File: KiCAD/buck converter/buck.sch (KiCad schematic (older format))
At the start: 17 parts, among them P1 VIN, P2 VOUT, Q1 Q_PMOS_DGS, U1 LTC1771

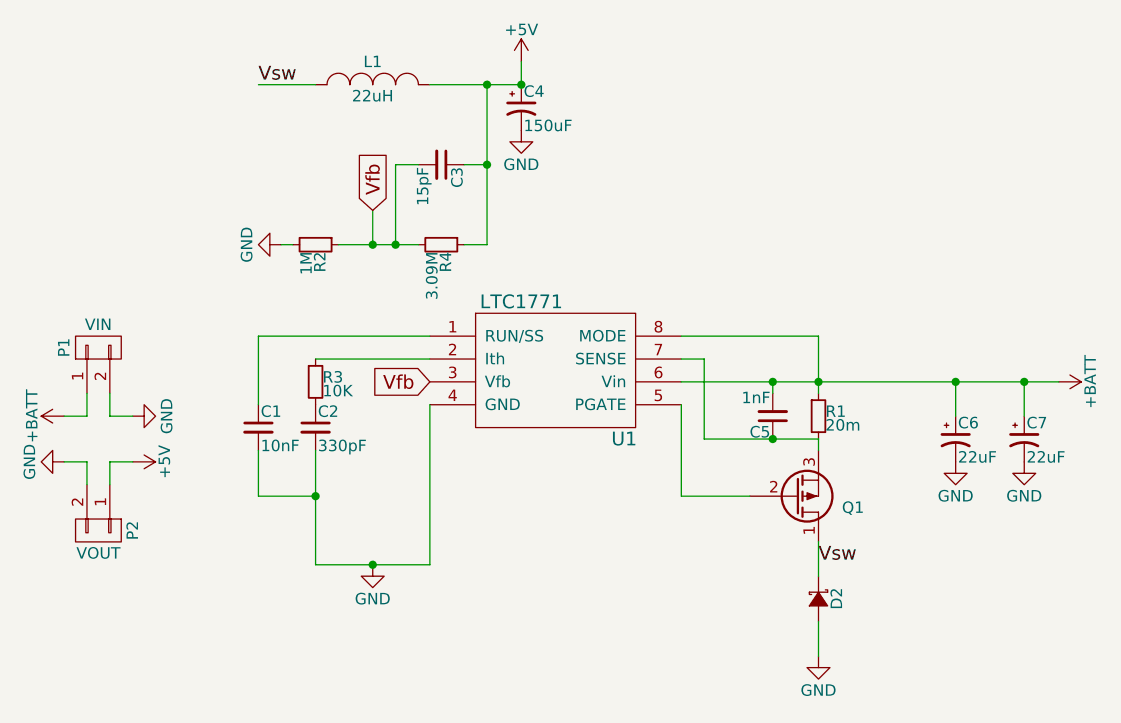
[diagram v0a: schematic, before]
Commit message: Improved the buck converter board layout
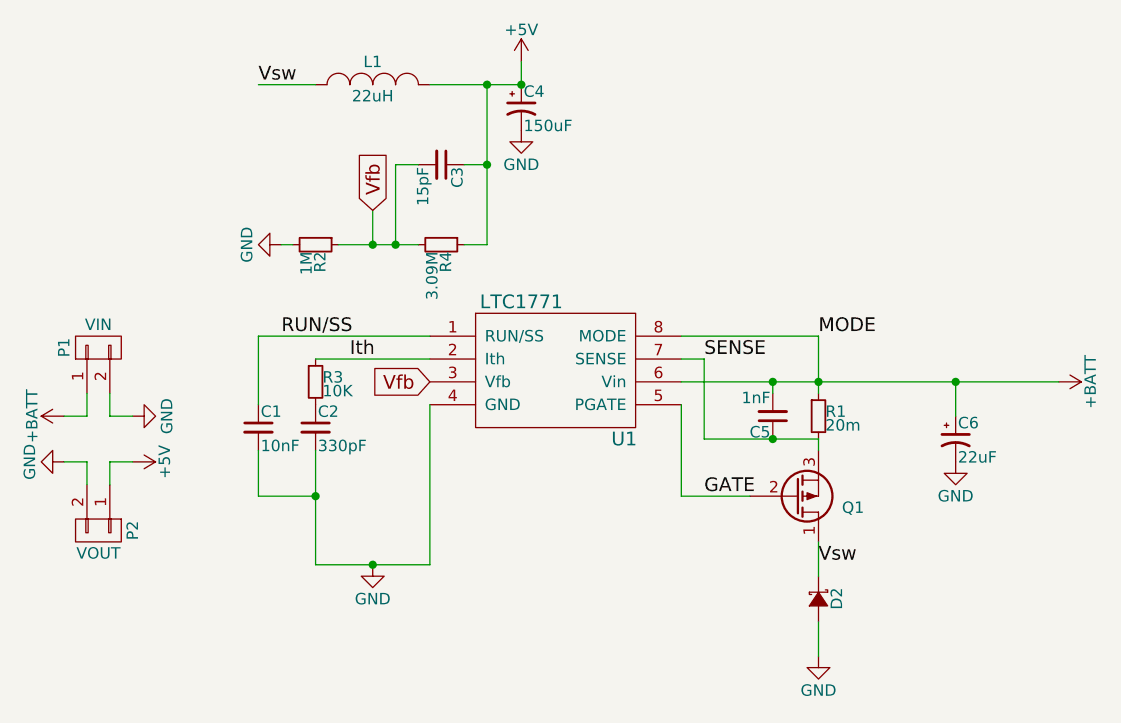
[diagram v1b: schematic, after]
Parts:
- removed C7: 22uF, Capacitors_SMD:CP_Elec_6.3x5.3, symbol CP1_Small
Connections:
- net SENSE: now reaches C5.1, Q1.3 (S), R1.2, U1.7 (SENSE)
- net GATE: now reaches Q1.2 (G), U1.5 (PGATE)
- net Ith: now reaches R3.1, U1.2 (Ith)
- net RUN/SS: now reaches C1.1, U1.1 (RUN/SS)
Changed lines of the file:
@@
-$EndComp
-$Comp
-L CP1_Small C7
-U 1 1 58964A17
-P 7800 4150
-F 0 "C7" H 7810 4220 50  0000 L CNN
-F 1 "22uF" H 7810 4070 50  0000 L CNN
-F 2 "Capacitors_SMD:CP_Elec_6.3x5.3" H 7800 4150 50  0001 C CNN
-F 3 "" H 7800 4150 50  0000 C CNN
-	1    7800 4150
-	1    0    0    -1
 $EndComp
 $Comp
@@
 	5200 4000 5200 4700
 Connection ~ 7500 3900
-Connection ~ 7800 3900
-Wire Wire Line
-	7800 4050 7800 3900
 Wire Wire Line
 	7500 3900 7500 4050
@@
 	1    0    0    -1
 $EndComp
-$Comp
-L GND #PWR07
-U 1 1 58966331
-P 7800 4250
-F 0 "#PWR07" H 7800 4000 50  0001 C CNN
-F 1 "GND" H 7800 4100 50  0000 C CNN
-F 2 "" H 7800 4250 50  0000 C CNN
-F 3 "" H 7800 4250 50  0000 C CNN
-	1    7800 4250
-	1    0    0    -1
-$EndComp
 Wire Wire Line
 	6300 3700 6900 3700
@@
 	1    0    0    -1
 $EndComp
+Text Label 6400 3800 0    60   ~ 0
+SENSE
+Text Label 6900 3700 0    60   ~ 0
+MODE
+Text Label 6400 4400 0    60   ~ 0
+GATE
+Text Label 4850 3800 0    60   ~ 0
+Ith
+Text Label 4550 3700 0    60   ~ 0
+RUN/SS
 $EndSCHEMATC

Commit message: Updated board layout
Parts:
- added JP1: BURST, Connectors:PINHEAD1-3, symbol Jumper_NC_Dual
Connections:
- net +BATT: now also JP1.3; no longer U1.8 (MODE)
- net GND: now also JP1.1
- new net MODE: JP1.2, U1.8 (MODE)
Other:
- moved on the sheet: C5
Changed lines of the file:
@@
 F 3 "" H 6900 4050 50  0000 C CNN
 	1    6900 4050
-	1    0    0    -1
+	1    0    0    1
 $EndComp
 $Comp
@@
 L C_Small C5
 U 1 1 58964849
-P 6700 4050
-F 0 "C5" H 6710 4120 50  0000 L CNN
-F 1 "1nF" H 6710 3970 50  0000 L CNN
-F 2 "Capacitors_SMD:C_0805_HandSoldering" H 6700 4050 50  0001 C CNN
-F 3 "" H 6700 4050 50  0000 C CNN
-	1    6700 4050
-	-1   0    0    1
+P 7250 3800
+F 0 "C5" H 7260 3870 50  0000 L CNN
+F 1 "1nF" H 7260 3720 50  0000 L CNN
+F 2 "Capacitors_SMD:C_0805_HandSoldering" H 7250 3800 50  0001 C CNN
+F 3 "" H 7250 3800 50  0000 C CNN
+	1    7250 3800
+	0    -1   -1   0
 $EndComp
 $Comp
@@
 Connection ~ 7500 3900
 Wire Wire Line
-	7500 3900 7500 4050
+	7500 3800 7500 4050
 Wire Wire Line
 	6300 4000 6300 4400
@@
 	6300 4400 6600 4400
 Wire Wire Line
-	6900 3700 6900 3950
-Connection ~ 6900 3900
-Wire Wire Line
-	6900 4150 6900 4200
-Wire Wire Line
-	6400 4150 6400 3800
-Wire Wire Line
-	6400 3800 6300 3800
+	6300 3800 7150 3800
 Wire Wire Line
 	6900 4750 6900 4600
 $Comp
-L GND #PWR06
+L GND #PWR05
 U 1 1 589662F9
 P 7500 4250
-F 0 "#PWR06" H 7500 4000 50  0001 C CNN
+F 0 "#PWR05" H 7500 4000 50  0001 C CNN
 F 1 "GND" H 7500 4100 50  0000 C CNN
 F 2 "" H 7500 4250 50  0000 C CNN
@@
 Wire Wire Line
 	6300 3700 6900 3700
-Connection ~ 6700 3900
-Wire Wire Line
-	6700 3950 6700 3900
-Wire Wire Line
-	6400 4150 6900 4150
-Connection ~ 6700 4150
 Wire Wire Line
 	4700 3800 5200 3800
@@
 Connection ~ 4950 3300
 $Comp
-L GND #PWR08
+L GND #PWR06
 U 1 1 58967FFD
 P 4550 3300
-F 0 "#PWR08" H 4550 3050 50  0001 C CNN
+F 0 "#PWR06" H 4550 3050 50  0001 C CNN
 F 1 "GND" H 4550 3150 50  0000 C CNN
 F 2 "" H 4550 3300 50  0000 C CNN
@@
 Connection ~ 5450 2600
 $Comp
-L GND #PWR09
+L GND #PWR07
 U 1 1 58968BDB
 P 5600 2800
-F 0 "#PWR09" H 5600 2550 50  0001 C CNN
+F 0 "#PWR07" H 5600 2550 50  0001 C CNN
 F 1 "GND" H 5600 2650 50  0000 C CNN
 F 2 "" H 5600 2800 50  0000 C CNN
@@
 	5200 2600 5600 2600
 $Comp
-L +5V #PWR010
+L +5V #PWR08
 U 1 1 58969042
 P 5600 2500
-F 0 "#PWR010" H 5600 2350 50  0001 C CNN
+F 0 "#PWR08" H 5600 2350 50  0001 C CNN
 F 1 "+5V" H 5600 2640 50  0000 C CNN
 F 2 "" H 5600 2500 50  0000 C CNN
@@
 	5600 2600 5600 2500
 $Comp
-L +5V #PWR011
+L +5V #PWR09
 U 1 1 589690C9
 P 3900 4250
-F 0 "#PWR011" H 3900 4100 50  0001 C CNN
+F 0 "#PWR09" H 3900 4100 50  0001 C CNN
 F 1 "+5V" H 3900 4390 50  0000 C CNN
 F 2 "" H 3900 4250 50  0000 C CNN
@@
 	3800 4250 3900 4250
 $Comp
-L GND #PWR012
+L GND #PWR010
 U 1 1 5896914A
 P 3600 4250
-F 0 "#PWR012" H 3600 4000 50  0001 C CNN
+F 0 "#PWR010" H 3600 4000 50  0001 C CNN
 F 1 "GND" H 3600 4100 50  0000 C CNN
 F 2 "" H 3600 4250 50  0000 C CNN
@@
 	6900 5100 6900 4950
 $Comp
-L GND #PWR05
+L GND #PWR011
 U 1 1 58965DDE
 P 6900 5100
-F 0 "#PWR05" H 6900 4850 50  0001 C CNN
+F 0 "#PWR011" H 6900 4850 50  0001 C CNN
 F 1 "GND" H 6900 4950 50  0000 C CNN
 F 2 "" H 6900 5100 50  0000 C CNN
@@
 Text Label 4550 3700 0    60   ~ 0
 RUN/SS
+$Comp
+L Jumper_NC_Dual JP1
+U 1 1 5898D624
+P 6900 3400
+F 0 "JP1" H 6950 3300 50  0000 L CNN
+F 1 "BURST" H 6900 3500 50  0000 C BNN
+F 2 "Connectors:PINHEAD1-3" H 6900 3400 50  0001 C CNN
+F 3 "" H 6900 3400 50  0000 C CNN
+	1    6900 3400
+	1    0    0    -1
+$EndComp
+$Comp
+L +BATT #PWR012
+U 1 1 5898D713
+P 7150 3400
+F 0 "#PWR012" H 7150 3250 50  0001 C CNN
+F 1 "+BATT" H 7150 3540 50  0000 C CNN
+F 2 "" H 7150 3400 50  0000 C CNN
+F 3 "" H 7150 3400 50  0000 C CNN
+	1    7150 3400
+	0    1    1    0
+$EndComp
+$Comp
+L GND #PWR013
+U 1 1 5898D751
+P 6650 3400
+F 0 "#PWR013" H 6650 3150 50  0001 C CNN
+F 1 "GND" H 6650 3250 50  0000 C CNN
+F 2 "" H 6650 3400 50  0000 C CNN
+F 3 "" H 6650 3400 50  0000 C CNN
+	1    6650 3400
+	0    1    1    0
+$EndComp
+Wire Wire Line
+	6900 3700 6900 3500
+Wire Wire Line
+	6900 3800 6900 3950
+Connection ~ 6900 3800
+Wire Wire Line
+	7350 3800 7500 3800
+Wire Wire Line
+	6900 4250 6900 4200
+Wire Wire Line
+	6900 4200 6500 4200
+Wire Wire Line
+	6500 4200 6500 3800
+Connection ~ 6500 3800
+Wire Wire Line
+	6900 4150 7300 4150
+Wire Wire Line
+	7300 4150 7300 3900
+Connection ~ 7300 3900
 $EndSCHEMATC

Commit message: Updated inductor footprint
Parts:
- L1: footprint Buck:inductor_th_10mm -> Buck:14mm-Inductor
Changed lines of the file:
@@
 F 0 "L1" H 4950 2700 50  0000 C CNN
 F 1 "22uH" H 4950 2550 50  0000 C CNN
-F 2 "Buck:inductor_th_10mm" H 4950 2600 50  0001 C CNN
+F 2 "Buck:14mm-Inductor" H 4950 2600 50  0001 C CNN
 F 3 "" H 4950 2600 50  0000 C CNN
 	1    4950 2600

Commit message: Updated schematic, PCB, amd BOM
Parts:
- removed JP1: BURST, Connectors:PINHEAD1-3, symbol Jumper_NC_Dual
- removed Q1: Q_PMOS_DGS, TO_SOT_Packages_SMD:SOT-23-6_Handsoldering, symbol Q_PMOS_DGS
- added U2: SI3421DV-T1-GE3, TO_SOT_Packages_SMD:SOT-23-6_Handsoldering, symbol SI3421DV-T1-GE3
- C4: value 150uF -> 330uF; footprint Capacitors_SMD:CP_Elec_6.3x5.8 -> Capacitors_SMD:CP_Elec_8x10
- D2: footprint Diodes_SMD:D_SOD-323_HandSoldering -> Diodes_SMD:D_SMB_Handsoldering
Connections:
- net MODE is gone; now on net GND: U1.8 (MODE)
- net GATE: now also U2.3 (G)
- net SENSE: now also U2.4 (S)
- net Vsw: now also U2.1 (D), U2.2 (D), U2.5 (D), U2.6 (D)
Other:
- moved on the sheet: D2
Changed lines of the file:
@@
 LIBS:roadrunner
 LIBS:tinkerforge
+LIBS:FET
 LIBS:buck-cache
 EELAYER 25 0
@@
 L D_Schottky_Small D2
 U 1 1 58962EBE
-P 6900 4850
-F 0 "D2" H 6850 4930 50  0000 L CNN
-F 1 "D_Schottky_Small" H 6620 4770 50  0001 L CNN
-F 2 "Diodes_SMD:D_SOD-323_HandSoldering" V 6900 4850 50  0001 C CNN
-F 3 "" V 6900 4850 50  0000 C CNN
-	1    6900 4850
-	0    1    1    0
+P 5900 4700
+F 0 "D2" H 5850 4780 50  0000 L CNN
+F 1 "D_Schottky_Small" H 5620 4620 50  0001 L CNN
+F 2 "Diodes_SMD:D_SMB_Handsoldering" V 5900 4700 50  0001 C CNN
+F 3 "" V 5900 4700 50  0000 C CNN
+	1    5900 4700
+	-1   0    0    1
 $EndComp
 $Comp
@@
 $EndComp
 $Comp
-L Q_PMOS_DGS Q1
-U 1 1 589631E9
-P 6800 4400
-F 0 "Q1" H 7100 4450 50  0000 R CNN
-F 1 "Q_PMOS_DGS" H 7450 4350 50  0001 R CNN
-F 2 "TO_SOT_Packages_SMD:SOT-23-6_Handsoldering" H 7000 4500 50  0001 C CNN
-F 3 "" H 6800 4400 50  0000 C CNN
-	1    6800 4400
-	1    0    0    1
-$EndComp
-$Comp
 L INDUCTOR_SMALL L1
 U 1 1 5896391B
@@
 P 5600 2700
 F 0 "C4" H 5610 2770 50  0000 L CNN
-F 1 "150uF" H 5610 2620 50  0000 L CNN
-F 2 "Capacitors_SMD:CP_Elec_6.3x5.8" H 5600 2700 50  0001 C CNN
+F 1 "330uF" H 5610 2620 50  0000 L CNN
+F 2 "Capacitors_SMD:CP_Elec_8x10" H 5600 2700 50  0001 C CNN
 F 3 "" H 5600 2700 50  0000 C CNN
 	1    5600 2700
@@
 	7500 3800 7500 4050
 Wire Wire Line
-	6300 4000 6300 4400
-Wire Wire Line
-	6300 4400 6600 4400
-Wire Wire Line
 	6300 3800 7150 3800
 Wire Wire Line
-	6900 4750 6900 4600
+	6000 4700 7150 4700
 $Comp
 L GND #PWR05
@@
 	5450 2950 5350 2950
 Connection ~ 5450 2950
-Text Label 6900 4700 0    60   ~ 0
+Text Label 6050 4700 3    60   ~ 0
 Vsw
 Wire Wire Line
@@
 	3700 4250 3600 4250
 Wire Wire Line
-	6900 5100 6900 4950
-$Comp
-L GND #PWR011
-U 1 1 58965DDE
-P 6900 5100
-F 0 "#PWR011" H 6900 4850 50  0001 C CNN
-F 1 "GND" H 6900 4950 50  0000 C CNN
-F 2 "" H 6900 5100 50  0000 C CNN
-F 3 "" H 6900 5100 50  0000 C CNN
-	1    6900 5100
-	1    0    0    -1
-$EndComp
+	5650 4700 5800 4700
 Text Label 6400 3800 0    60   ~ 0
 SENSE
 Text Label 6900 3700 0    60   ~ 0
 MODE
-Text Label 6400 4400 0    60   ~ 0
-GATE
 Text Label 4850 3800 0    60   ~ 0
 Ith
@@
 RUN/SS
 $Comp
-L Jumper_NC_Dual JP1
-U 1 1 5898D624
-P 6900 3400
-F 0 "JP1" H 6950 3300 50  0000 L CNN
-F 1 "BURST" H 6900 3500 50  0000 C BNN
-F 2 "Connectors:PINHEAD1-3" H 6900 3400 50  0001 C CNN
-F 3 "" H 6900 3400 50  0000 C CNN
-	1    6900 3400
-	1    0    0    -1
-$EndComp
-$Comp
-L +BATT #PWR012
-U 1 1 5898D713
-P 7150 3400
-F 0 "#PWR012" H 7150 3250 50  0001 C CNN
-F 1 "+BATT" H 7150 3540 50  0000 C CNN
-F 2 "" H 7150 3400 50  0000 C CNN
-F 3 "" H 7150 3400 50  0000 C CNN
-	1    7150 3400
-	0    1    1    0
-$EndComp
-$Comp
-L GND #PWR013
+L GND #PWR011
 U 1 1 5898D751
-P 6650 3400
-F 0 "#PWR013" H 6650 3150 50  0001 C CNN
-F 1 "GND" H 6650 3250 50  0000 C CNN
-F 2 "" H 6650 3400 50  0000 C CNN
-F 3 "" H 6650 3400 50  0000 C CNN
-	1    6650 3400
-	0    1    1    0
+P 6900 3500
+F 0 "#PWR011" H 6900 3250 50  0001 C CNN
+F 1 "GND" H 6900 3350 50  0000 C CNN
+F 2 "" H 6900 3500 50  0000 C CNN
+F 3 "" H 6900 3500 50  0000 C CNN
+	1    6900 3500
+	-1   0    0    1
 $EndComp
 Wire Wire Line
@@
 	7350 3800 7500 3800
 Wire Wire Line
-	6900 4250 6900 4200
-Wire Wire Line
-	6900 4200 6500 4200
-Wire Wire Line
-	6500 4200 6500 3800
+	6500 3800 6500 4250
 Connection ~ 6500 3800
 Wire Wire Line
@@
 	7300 4150 7300 3900
 Connection ~ 7300 3900
+$Comp
+L GND #PWR012
+U 1 1 58965DDE
+P 5650 4700
+F 0 "#PWR012" H 5650 4450 50  0001 C CNN
+F 1 "GND" H 5650 4550 50  0000 C CNN
+F 2 "" H 5650 4700 50  0000 C CNN
+F 3 "" H 5650 4700 50  0000 C CNN
+	1    5650 4700
+	0    1    1    0
+$EndComp
+$Comp
+L SI3421DV-T1-GE3 U2
+U 1 1 58D46DD3
+P 6800 5050
+F 0 "U2" H 6700 5250 60  0000 C CNN
+F 1 "SI3421DV-T1-GE3" H 6800 4850 60  0000 C CNN
+F 2 "TO_SOT_Packages_SMD:SOT-23-6_Handsoldering" H 6800 4800 60  0001 C CNN
+F 3 "" H 6800 4800 60  0001 C CNN
+	1    6800 5050
+	1    0    0    -1
+$EndComp
+Wire Wire Line
+	6300 4000 6300 5150
+Wire Wire Line
+	6300 5150 6450 5150
+Text Label 6300 5150 0    60   ~ 0
+GATE
+Wire Wire Line
+	6450 4700 6450 5050
+Connection ~ 6450 4950
+Wire Wire Line
+	7150 4700 7150 5050
+Connection ~ 6450 4700
+Connection ~ 7150 4950
+Wire Wire Line
+	7150 5150 7300 5150
+Wire Wire Line
+	7300 5150 7300 4250
+Wire Wire Line
+	7300 4250 6500 4250
 $EndSCHEMATC

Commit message: Board design updated
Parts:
- added C7: 100nF, Capacitors_SMD:C_0805_HandSoldering, symbol C_Small
- C4: value 330uF -> 150uF; footprint Capacitors_SMD:CP_Elec_8x10 -> Capacitors_SMD:CP_Elec_6.3x7.7
- C6: value 22uF -> 56uF; footprint Capacitors_SMD:CP_Elec_6.3x5.3 -> Capacitors_SMD:CP_Elec_5x5.7
- D2: footprint Diodes_SMD:D_SMB_Handsoldering -> Diodes_SMD:D_SMA_Handsoldering
- R1: value 20m -> 33m
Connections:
- net +BATT: now also C7.1
- net GND: now also C7.2
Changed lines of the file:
@@
 F 0 "D2" H 5850 4780 50  0000 L CNN
 F 1 "D_Schottky_Small" H 5620 4620 50  0001 L CNN
-F 2 "Diodes_SMD:D_SMB_Handsoldering" V 5900 4700 50  0001 C CNN
+F 2 "Diodes_SMD:D_SMA_Handsoldering" V 5900 4700 50  0001 C CNN
 F 3 "" V 5900 4700 50  0000 C CNN
 	1    5900 4700
@@
 P 6900 4050
 F 0 "R1" H 6930 4070 50  0000 L CNN
-F 1 "20m" H 6930 4010 50  0000 L CNN
+F 1 "33m" H 6930 4010 50  0000 L CNN
 F 2 "Resistors_SMD:R_1206_HandSoldering" H 6900 4050 50  0001 C CNN
 F 3 "" H 6900 4050 50  0000 C CNN
@@
 P 7500 4150
 F 0 "C6" H 7510 4220 50  0000 L CNN
-F 1 "22uF" H 7510 4070 50  0000 L CNN
-F 2 "Capacitors_SMD:CP_Elec_6.3x5.3" H 7500 4150 50  0001 C CNN
+F 1 "56uF" H 7510 4070 50  0000 L CNN
+F 2 "Capacitors_SMD:CP_Elec_5x5.7" H 7500 4150 50  0001 C CNN
 F 3 "" H 7500 4150 50  0000 C CNN
 	1    7500 4150
@@
 P 5600 2700
 F 0 "C4" H 5610 2770 50  0000 L CNN
-F 1 "330uF" H 5610 2620 50  0000 L CNN
-F 2 "Capacitors_SMD:CP_Elec_8x10" H 5600 2700 50  0001 C CNN
+F 1 "150uF" H 5610 2620 50  0000 L CNN
+F 2 "Capacitors_SMD:CP_Elec_6.3x7.7" H 5600 2700 50  0001 C CNN
 F 3 "" H 5600 2700 50  0000 C CNN
 	1    5600 2700
@@
 	3700 4050 3600 4050
 $Comp
-L GND #PWR01
+L GND #PWR3
 U 1 1 58964DDE
 P 3900 4050
-F 0 "#PWR01" H 3900 3800 50  0001 C CNN
+F 0 "#PWR3" H 3900 3800 50  0001 C CNN
 F 1 "GND" H 3900 3900 50  0000 C CNN
 F 2 "" H 3900 4050 50  0000 C CNN
@@
 $EndComp
 $Comp
-L +BATT #PWR02
+L +BATT #PWR1
 U 1 1 58964E10
 P 3600 4050
-F 0 "#PWR02" H 3600 3900 50  0001 C CNN
+F 0 "#PWR1" H 3600 3900 50  0001 C CNN
 F 1 "+BATT" H 3600 4190 50  0000 C CNN
 F 2 "" H 3600 4050 50  0000 C CNN
@@
 $EndComp
 $Comp
-L +BATT #PWR03
+L +BATT #PWR13
 U 1 1 5896507A
 P 7950 3900
-F 0 "#PWR03" H 7950 3750 50  0001 C CNN
+F 0 "#PWR13" H 7950 3750 50  0001 C CNN
 F 1 "+BATT" H 7950 4040 50  0000 C CNN
 F 2 "" H 7950 3900 50  0000 C CNN
@@
 	6300 3900 7950 3900
 $Comp
-L GND #PWR04
+L GND #PWR6
 U 1 1 589650C7
 P 4950 4700
-F 0 "#PWR04" H 4950 4450 50  0001 C CNN
+F 0 "#PWR6" H 4950 4450 50  0001 C CNN
 F 1 "GND" H 4950 4550 50  0000 C CNN
 F 2 "" H 4950 4700 50  0000 C CNN
@@
 	6000 4700 7150 4700
 $Comp
-L GND #PWR05
+L GND #PWR11
 U 1 1 589662F9
 P 7500 4250
-F 0 "#PWR05" H 7500 4000 50  0001 C CNN
+F 0 "#PWR11" H 7500 4000 50  0001 C CNN
 F 1 "GND" H 7500 4100 50  0000 C CNN
 F 2 "" H 7500 4250 50  0000 C CNN
@@
 Connection ~ 4950 3300
 $Comp
-L GND #PWR06
+L GND #PWR5
 U 1 1 58967FFD
 P 4550 3300
-F 0 "#PWR06" H 4550 3050 50  0001 C CNN
+F 0 "#PWR5" H 4550 3050 50  0001 C CNN
 F 1 "GND" H 4550 3150 50  0000 C CNN
 F 2 "" H 4550 3300 50  0000 C CNN
@@
 Connection ~ 5450 2600
 $Comp
-L GND #PWR07
+L GND #PWR8
 U 1 1 58968BDB
 P 5600 2800
-F 0 "#PWR07" H 5600 2550 50  0001 C CNN
+F 0 "#PWR8" H 5600 2550 50  0001 C CNN
 F 1 "GND" H 5600 2650 50  0000 C CNN
 F 2 "" H 5600 2800 50  0000 C CNN
@@
 	5200 2600 5600 2600
 $Comp
-L +5V #PWR08
+L +5V #PWR7
 U 1 1 58969042
 P 5600 2500
-F 0 "#PWR08" H 5600 2350 50  0001 C CNN
+F 0 "#PWR7" H 5600 2350 50  0001 C CNN
 F 1 "+5V" H 5600 2640 50  0000 C CNN
 F 2 "" H 5600 2500 50  0000 C CNN
@@
 	5600 2600 5600 2500
 $Comp
-L +5V #PWR09
+L +5V #PWR4
 U 1 1 589690C9
 P 3900 4250
-F 0 "#PWR09" H 3900 4100 50  0001 C CNN
+F 0 "#PWR4" H 3900 4100 50  0001 C CNN
 F 1 "+5V" H 3900 4390 50  0000 C CNN
 F 2 "" H 3900 4250 50  0000 C CNN
@@
 	3800 4250 3900 4250
 $Comp
-L GND #PWR010
+L GND #PWR2
 U 1 1 5896914A
 P 3600 4250
-F 0 "#PWR010" H 3600 4000 50  0001 C CNN
+F 0 "#PWR2" H 3600 4000 50  0001 C CNN
 F 1 "GND" H 3600 4100 50  0000 C CNN
 F 2 "" H 3600 4250 50  0000 C CNN
@@
 RUN/SS
 $Comp
-L GND #PWR011
+L GND #PWR10
 U 1 1 5898D751
 P 6900 3500
-F 0 "#PWR011" H 6900 3250 50  0001 C CNN
+F 0 "#PWR10" H 6900 3250 50  0001 C CNN
 F 1 "GND" H 6900 3350 50  0000 C CNN
 F 2 "" H 6900 3500 50  0000 C CNN
@@
 Connection ~ 7300 3900
 $Comp
-L GND #PWR012
+L GND #PWR9
 U 1 1 58965DDE
 P 5650 4700
-F 0 "#PWR012" H 5650 4450 50  0001 C CNN
+F 0 "#PWR9" H 5650 4450 50  0001 C CNN
 F 1 "GND" H 5650 4550 50  0000 C CNN
 F 2 "" H 5650 4700 50  0000 C CNN
@@
 Wire Wire Line
 	7300 4250 6500 4250
+$Comp
+L C_Small C7
+U 1 1 58E148D1
+P 7800 4150
+F 0 "C7" H 7810 4220 50  0000 L CNN
+F 1 "100nF" H 7810 4070 50  0000 L CNN
+F 2 "Capacitors_SMD:C_0805_HandSoldering" H 7800 4150 50  0001 C CNN
+F 3 "" H 7800 4150 50  0000 C CNN
+	1    7800 4150
+	1    0    0    -1
+$EndComp
+Wire Wire Line
+	7800 4050 7800 3900
+Connection ~ 7800 3900
+$Comp
+L GND #PWR12
+U 1 1 58E149CA
+P 7800 4250
+F 0 "#PWR12" H 7800 4000 50  0001 C CNN
+F 1 "GND" H 7800 4100 50  0000 C CNN
+F 2 "" H 7800 4250 50  0000 C CNN
+F 3 "" H 7800 4250 50  0000 C CNN
+	1    7800 4250
+	1    0    0    -1
+$EndComp
 $EndSCHEMATC
